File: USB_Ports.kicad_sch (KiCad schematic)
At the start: 30 parts, among them IC2 TPS2066TDGNRQ1, IC3 TPS2066TDGNRQ1, J10 3-2172091-2, J5 3-2172091-2, J6 3-2172091-2, J8 3-2172091-2

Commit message: small changes for ravi
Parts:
- added F3, F4: 500mA, symbol Device:Fuse
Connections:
- net VBUS3: now also F3.2; no longer IC3.7 (OUT1)
- net VBUS4: now also F4.2; no longer IC3.6 (OUT2)
- new net: F4.1, IC3.6 (OUT2)
- new net: F3.1, IC3.7 (OUT1)
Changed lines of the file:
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@@
 	(wire
 		(pts
-			(xy 99.06 121.92) (xy 111.76 121.92)
+			(xy 99.06 121.92) (xy 100.33 121.92)
 		)
 		(stroke
@@
 	(wire
 		(pts
-			(xy 99.06 114.3) (xy 111.76 114.3)
+			(xy 99.06 114.3) (xy 100.33 114.3)
 		)
 		(stroke
@@
 	(wire
 		(pts
+			(xy 107.95 121.92) (xy 115.57 121.92)
+		)
+		(stroke
+			(width 0)
+			(type default)
+		)
+	)
+	(wire
+		(pts
 			(xy 228.6 133.35) (xy 228.6 134.62)
 		)
@@
 	(wire
 		(pts
+			(xy 107.95 114.3) (xy 115.57 114.3)
+		)
+		(stroke
+			(width 0)
+			(type default)
+		)
+	)
+	(wire
+		(pts
 			(xy 232.41 105.41) (xy 255.27 105.41)
 		)
@@
 	)
 	(label "VBUS3"
-		(at 111.76 114.3 180)
+		(at 115.57 114.3 180)
 		(fields_autoplaced yes)
 		(effects
@@
 	)
 	(label "VBUS4"
-		(at 111.76 121.92 180)
+		(at 115.57 121.92 180)
 		(fields_autoplaced yes)
 		(effects
@@
 	)
 	(symbol
+		(lib_id "Device:Fuse")
+		(at 104.14 121.92 90)
+		(unit 1)
+		(exclude_from_sim no)
+		(in_bom yes)
+		(on_board yes)
+		(dnp no)
+		(property "Reference" "F4"
+			(at 100.076 119.38 90)
+			(effects
+				(font
+					(size 1.27 1.27)
+				)
+			)
+		)
+		(property "Value" "500mA"
+			(at 105.918 119.634 90)
+			(effects
+				(font
+					(size 1.27 1.27)
+				)
+			)
+		)
+		(property "Footprint" ""
+			(at 104.14 123.698 90)
+			(effects
+				(font
+					(size 1.27 1.27)
+				)
+				(hide yes)
+			)
+		)
+		(property "Datasheet" "~"
+			(at 104.14 121.92 0)
+			(effects
+				(font
+					(size 1.27 1.27)
+				)
+				(hide yes)
+			)
+		)
+		(property "Description" "Fuse"
+			(at 104.14 121.92 0)
+			(effects
+				(font
+					(size 1.27 1.27)
+				)
+				(hide yes)
+			)
+		)
+		(pin "1"
+		)
+		(pin "2"
+		)
+		(instances
+			(project "PiBoard"
+				(path "/e4d65698-b8ec-4bf6-9f2b-a5010377155a/ba481c31-e70b-40cd-84a6-4c7235d9d730/9db2d452-e488-4d0d-9fba-1e3727141806"
+					(reference "F4")
+					(unit 1)
+				)
+			)
+		)
+	)
+	(symbol
+		(lib_id "power:GNDPWR")
+		(at 190.5 78.74 0)
+		(unit 1)
+		(exclude_from_sim no)
+		(in_bom yes)
+		(on_board yes)
+		(dnp no)
+		(fields_autoplaced yes)
+		(property "Reference" "#PWR027"
+			(at 190.5 83.82 0)
+			(effects
+				(font
+					(size 1.27 1.27)
+				)
+				(hide yes)
+			)
+		)
+		(property "Value" "GNDPWR"
+			(at 190.373 82.55 0)
+			(effects
+				(font
+					(size 1.27 1.27)
+				)
+			)
+		)
+		(property "Footprint" ""
+			(at 190.5 80.01 0)
+			(effects
+				(font
+					(size 1.27 1.27)
+				)
+				(hide yes)
+			)
+		)
+		(property "Datasheet" ""
+			(at 190.5 80.01 0)
+			(effects
+				(font
+					(size 1.27 1.27)
+				)
+				(hide yes)
+			)
+		)
+		(property "Description" "Power symbol creates a global label with name \"GNDPWR\" , global ground"
+			(at 190.5 78.74 0)
+			(effects
+				(font
+					(size 1.27 1.27)
+				)
+				(hide yes)
+			)
+		)
+		(pin "1"
+		)
+		(instances
+			(project ""
+				(path "/e4d65698-b8ec-4bf6-9f2b-a5010377155a/ba481c31-e70b-40cd-84a6-4c7235d9d730/9db2d452-e488-4d0d-9fba-1e3727141806"
+					(reference "#PWR027")
+					(unit 1)
+				)
+			)
+		)
+	)
+	(symbol
 		(lib_id "power:GND")
 		(at 167.64 115.57 0)
@@
 	)
 	(symbol
+		(lib_id "Device:Fuse")
+		(at 104.14 114.3 90)
+		(unit 1)
+		(exclude_from_sim no)
+		(in_bom yes)
+		(on_board yes)
+		(dnp no)
+		(fields_autoplaced yes)
+		(property "Reference" "F3"
+			(at 104.14 107.95 90)
+			(effects
+				(font
+					(size 1.27 1.27)
+				)
+			)
+		)
+		(property "Value" "500mA"
+			(at 104.14 110.49 90)
+			(effects
+				(font
+					(size 1.27 1.27)
+				)
+			)
+		)
+		(property "Footprint" ""
+			(at 104.14 116.078 90)
+			(effects
+				(font
+					(size 1.27 1.27)
+				)
+				(hide yes)
+			)
+		)
+		(property "Datasheet" "~"
+			(at 104.14 114.3 0)
+			(effects
+				(font
+					(size 1.27 1.27)
+				)
+				(hide yes)
+			)
+		)
+		(property "Description" "Fuse"
+			(at 104.14 114.3 0)
+			(effects
+				(font
+					(size 1.27 1.27)
+				)
+				(hide yes)
+			)
+		)
+		(pin "1"
+		)
+		(pin "2"
+		)
+		(instances
+			(project "PiBoard"
+				(path "/e4d65698-b8ec-4bf6-9f2b-a5010377155a/ba481c31-e70b-40cd-84a6-4c7235d9d730/9db2d452-e488-4d0d-9fba-1e3727141806"
+					(reference "F3")
+					(unit 1)
+				)
+			)
+		)
+	)
+	(symbol
 		(lib_id "Device:C")
 		(at 232.41 109.22 0)
@@
 					(unit 1)
 				)
-			)
-		)
-	)
-	(symbol
-		(lib_id "power:GNDPWR")
-		(at 190.5 78.74 0)
-		(unit 1)
-		(exclude_from_sim no)
-		(in_bom yes)
-		(on_board yes)
-		(dnp no)
-		(fields_autoplaced yes)
-		(property "Reference" "#PWR027"
-			(at 190.5 83.82 0)
-			(effects
-				(font
-					(size 1.27 1.27)
-				)
-				(hide yes)
-			)
-		)
-		(property "Value" "GNDPWR"
-			(at 190.373 82.55 0)
-			(effects
-				(font
-					(size 1.27 1.27)
-				)
-			)
-		)
-		(property "Footprint" ""
-			(at 190.5 80.01 0)
-			(effects
-				(font
-					(size 1.27 1.27)
-				)
-				(hide yes)
-			)
-		)
-		(property "Datasheet" ""
-			(at 190.5 80.01 0)
-			(effects
-				(font
-					(size 1.27 1.27)
-				)
-				(hide yes)
-			)
-		)
-		(property "Description" "Power symbol creates a global label with name \"GNDPWR\" , global ground"
-			(at 190.5 78.74 0)
-			(effects
-				(font
-					(size 1.27 1.27)
-				)
-				(hide yes)
-			)
-		)
-		(pin "1"
-		)
-		(instances
-			(project ""
-				(path "/e4d65698-b8ec-4bf6-9f2b-a5010377155a/ba481c31-e70b-40cd-84a6-4c7235d9d730/9db2d452-e488-4d0d-9fba-1e3727141806"
-					(reference "#PWR027")
-					(unit 1)
-				)

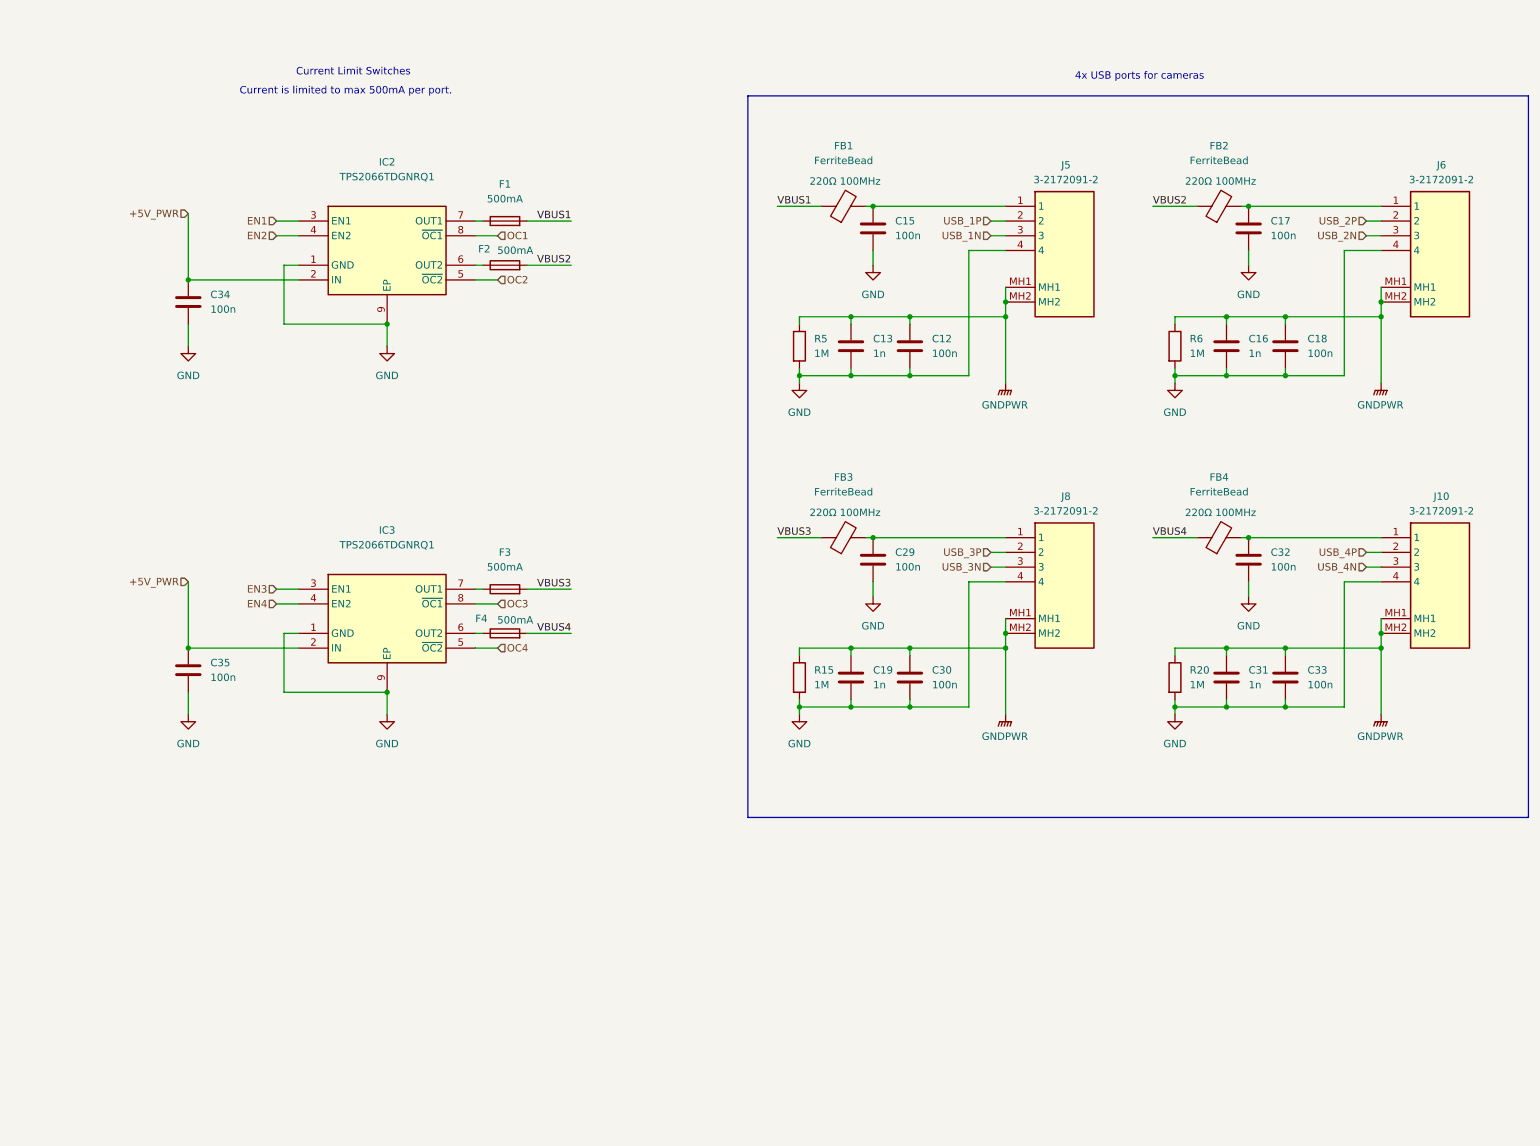
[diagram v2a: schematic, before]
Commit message: added parts to almost everything (except can xtal and fuses)
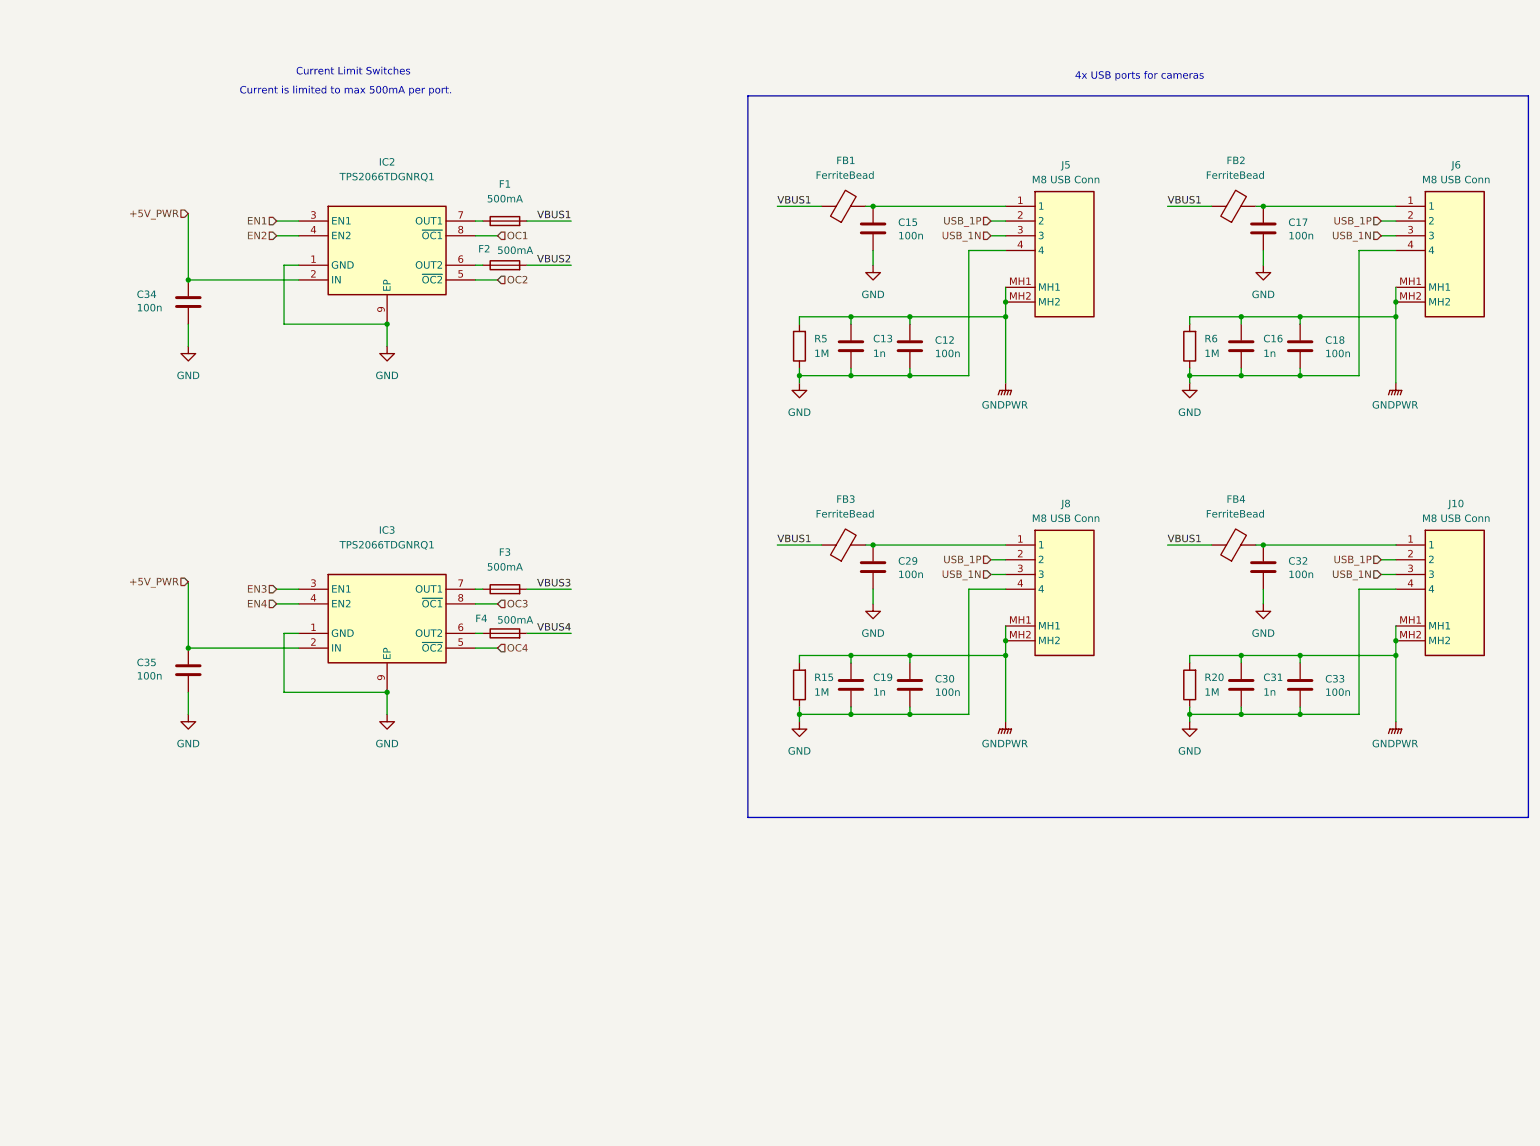
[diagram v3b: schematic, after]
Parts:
- C12, C15, C17, C18, C29, C30, C32, C33, C34, C35: footprint (none) -> Capacitor_SMD:C_0805_2012Metric; P/N (none) -> C0805C104M5RACTU
- C13, C16, C19, C31: footprint (none) -> Capacitor_SMD:C_0805_2012Metric; P/N (none) -> C0805C102J5HACAUTO
- FB1, FB2, FB3, FB4: footprint (none) -> Inductor_SMD:L_1206_3216Metric; P/N (none) -> BMC-Q2CY0220H; Part # BMC-Q2CY0220H -> (none); Spec 220Ω 100MHz -> (none)
- IC2, IC3: Height 1.1 -> (none); Manufacturer_Name Texas Instruments -> (none); Manufacturer_Part_Number TPS2066TDGNRQ1 -> (none); Mouser Part Number 595-TPS2066TDGNRQ1 -> (none); Mouser Price/Stock https://www.mouser.co.uk/ProductDetail/Texas-Instruments/TP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 -> (none); P/N (none) -> TPS2066TDGNRQ1
- J10, J5, J6, J8: value 3-2172091-2 -> M8 USB Conn; Arrow Part Number 3-2172091-2 -> (none); Arrow Price/Stock https://www.arrow.com/en/products/3-2172091-2/te-connectivi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 -> (none); Height 12.6 -> (none); Manufacturer_Name TE Connectivity -> (none); Manufacturer_Part_Number 3-2172091-2 -> (none); Mouser Part Number 571-3-2172091-2 -> (none); Mouser Price/Stock https://www.mouser.co.uk/ProductDetail/TE-Connectivity/3-21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 -> (none); P/N (none) -> 3-2172091-2
- R15, R20, R5, R6: footprint (none) -> Resistor_SMD:R_0805_2012Metric; P/N (none) -> CRCW08051M00FKEA
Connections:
- net USB_2N is gone; now on net USB_1N: J6.3
- net USB_2P is gone; now on net USB_1P: J6.2
- net USB_3N is gone; now on net USB_1N: J8.3
- net USB_3P is gone; now on net USB_1P: J8.2
- net USB_4N is gone; now on net USB_1N: J10.3
- net USB_4P is gone; now on net USB_1P: J10.2
- net GND: now also R15.1, R20.1, R5.1, R6.1; no longer R15.2, R20.2, R5.2, R6.2
- net GNDPWR: now also R15.2, R20.2, R5.2, R6.2; no longer R15.1, R20.1, R5.1, R6.1
- net VBUS1: now also FB2.1, FB3.1, FB4.1
- net VBUS2: no longer FB2.1
- net VBUS3: no longer FB3.1
- net VBUS4: no longer FB4.1

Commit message: fixed cap sizes, added remaining parts, fixed rtc battery
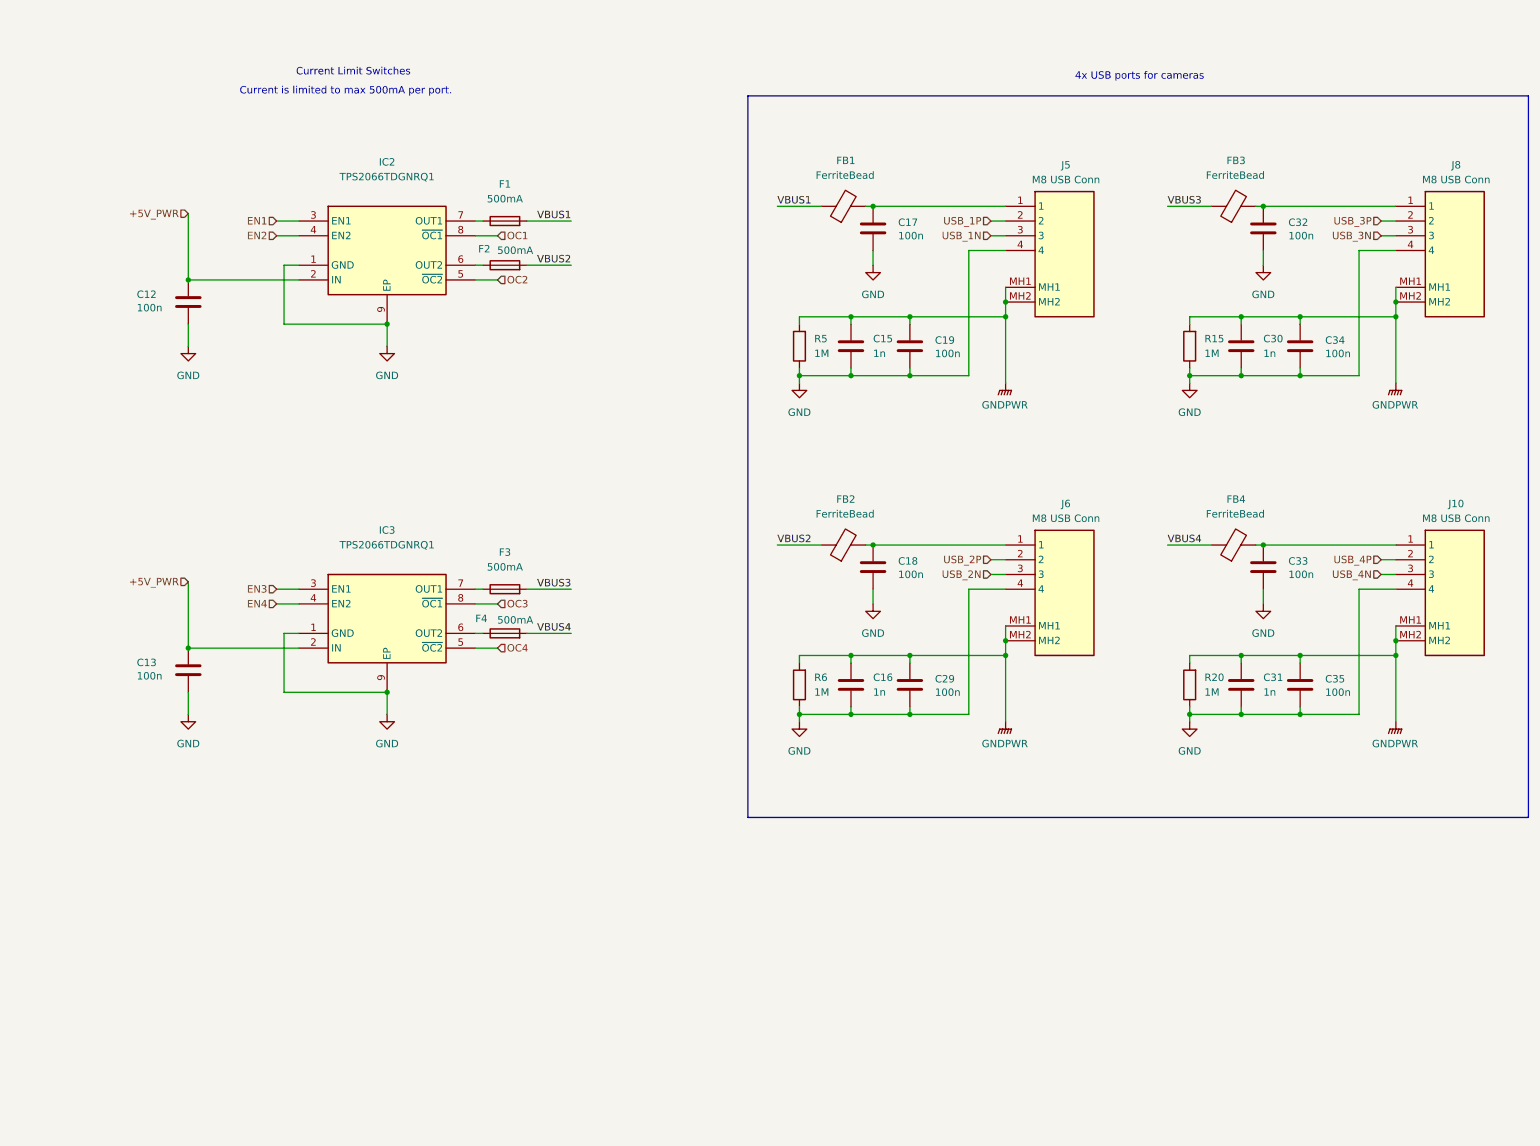
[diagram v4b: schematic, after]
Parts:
- F1, F2, F3, F4: footprint (none) -> Fuse:Fuse_1206_3216Metric; P/N (none) -> 0440.500WR
- IC2, IC3: footprint SOP65P490X110-9N -> Controls_Pi:SOP65P490X110-9N
- J10, J5: footprint 321720912 -> Controls_Pi:321720912
- J6: renamed from J8; footprint 321720912 -> Controls_Pi:321720912
- J8: renamed from J6; footprint 321720912 -> Controls_Pi:321720912
- renumbered C34 to C12, C35 to C13, C13 to C15, C19 to C16, C15 to C17, C29 to C18, C12 to C19, C30 to C29, C16 to C30, C17 to C32, C32 to C33, C18 to C34, C33 to C35, FB3 to FB2, FB2 to FB3, R6 to R15, R15 to R6
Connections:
- net USB_1N: no longer J10.3, J6.3, J8.3
- net USB_1P: no longer J10.2, J6.2, J8.2
- net VBUS1: no longer FB2.1, FB3.1, FB4.1
- net VBUS2: now also FB2.1
- net VBUS3: now also FB3.1
- net VBUS4: now also FB4.1
- new net USB_2N: J6.3
- new net USB_2P: J6.2
- new net USB_3N: J8.3
- new net USB_3P: J8.2
- new net USB_4N: J10.3
- new net USB_4P: J10.2

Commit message: review committee changes implmented
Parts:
- added U6, U7: TPD4EUSB30, Package_SON:USON-10_2.5x1.0mm_P0.5mm, symbol Power_Protection:TPD4EUSB30
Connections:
- net GND: now also U6.3 (GND), U6.8 (GND), U7.3 (GND), U7.8 (GND)
- net USB_1N: now also U6.2 (D1-)
- net USB_1P: now also U6.1 (D1+)
- net USB_2N: now also U6.5 (D2-)
- net USB_2P: now also U6.4 (D2+)
- net USB_3N: now also U7.2 (D1-)
- net USB_3P: now also U7.1 (D1+)
- net USB_4N: now also U7.5 (D2-)
- net USB_4P: now also U7.4 (D2+)
- no-connect marks 0 -> 8
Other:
- note added: "USB ESD Protection"
- moved on the sheet: C13, F3, F4, IC3
